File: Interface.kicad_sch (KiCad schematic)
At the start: 62 parts, among them U11 WE-TVS-82400102, U13 WE-TVS-82400102, U2 SN74LVC2G14DBV, U4 SN74LVC2G14DBV, U5 SN74LVC2G14DBV, U6 THVD1400D, U7 TLP2310, U8 TLP2310

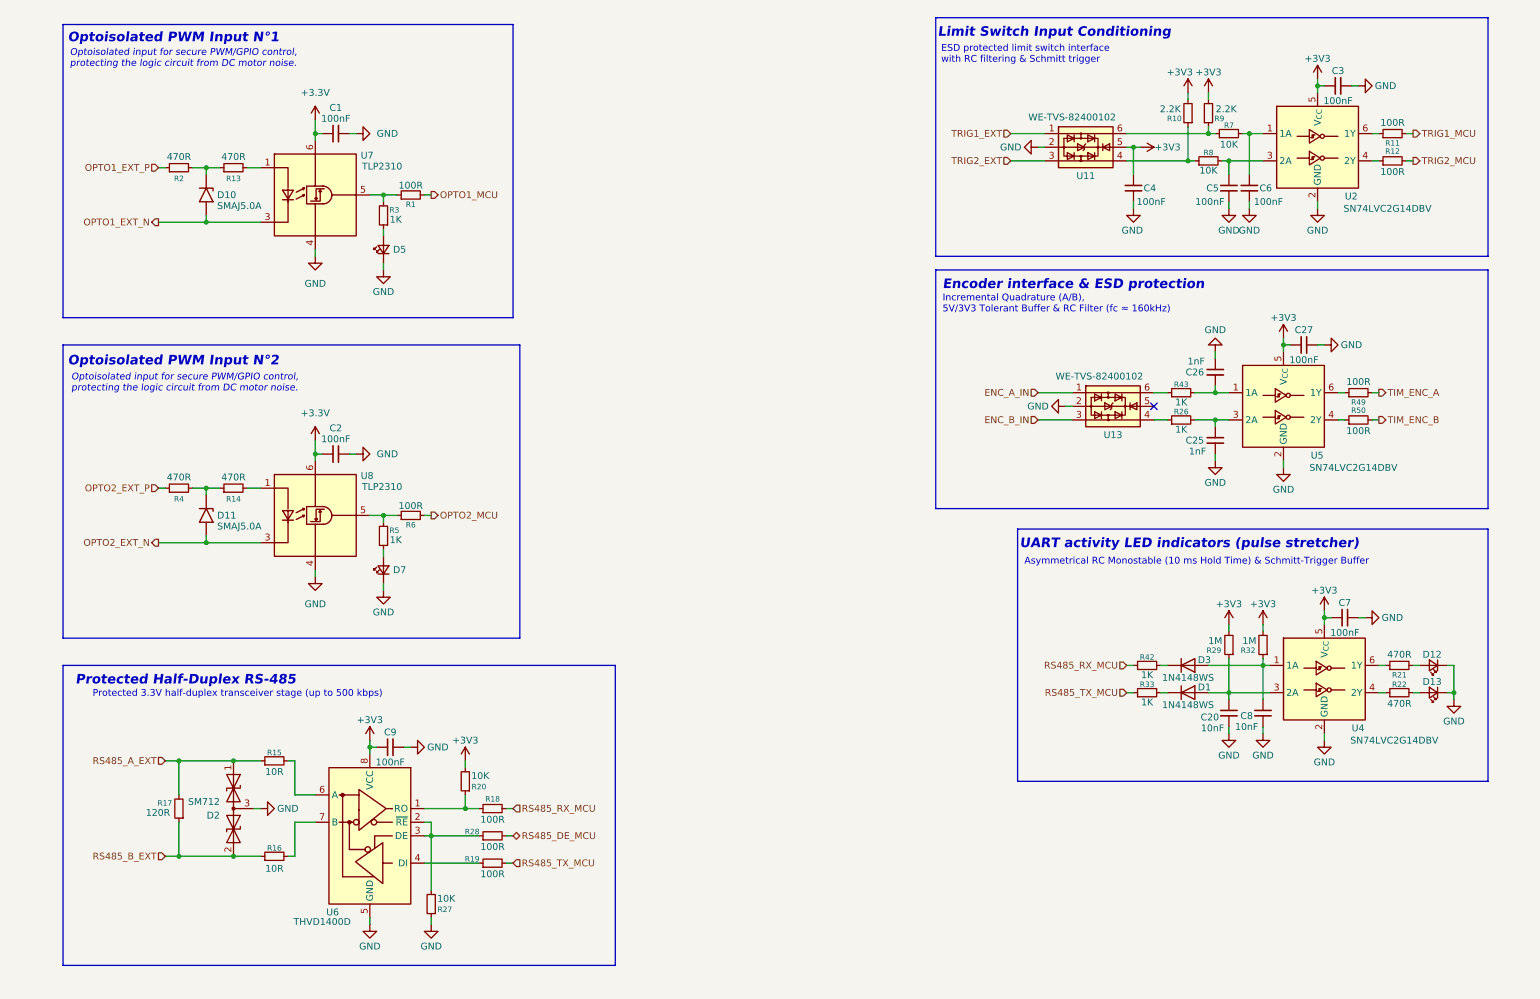
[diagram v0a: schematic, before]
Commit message: feat: add standardized functional notes across all schematic sheets
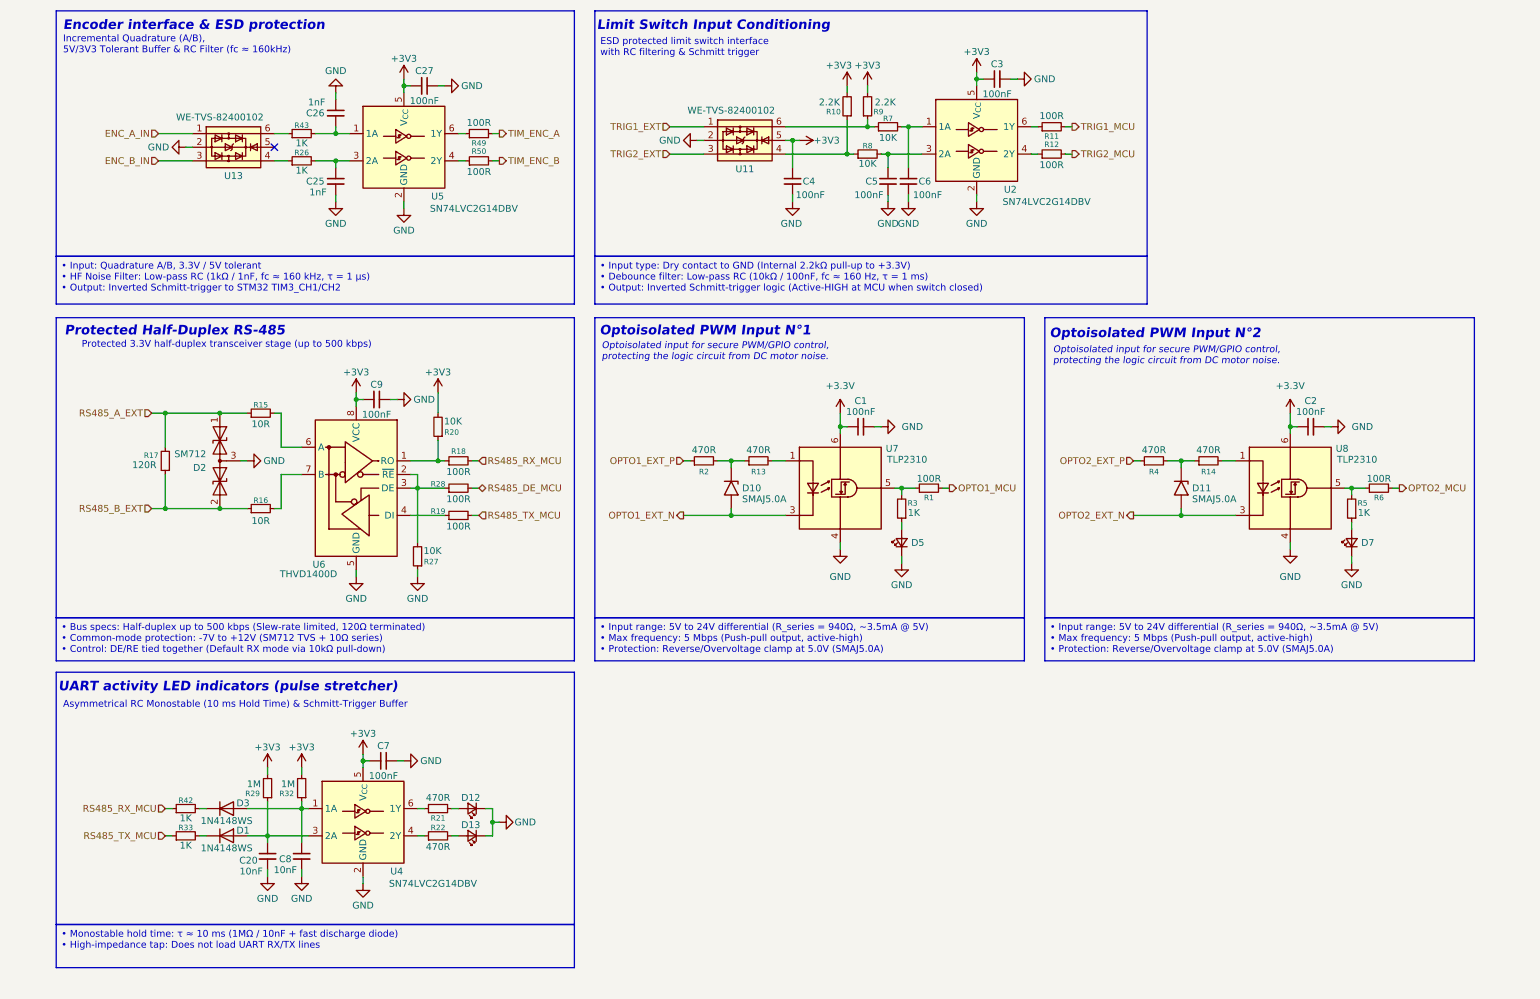
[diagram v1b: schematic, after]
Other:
- moved on the sheet: C1, C2, C20, C25, C26, C27, C3, C4, C5, C6, C7, C8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

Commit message: fix: fix some errors in shematic
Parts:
- D6: renamed from D10; value SMAJ5.0A -> SMAJ6.0A
- D8: renamed from D11; value SMAJ5.0A -> SMAJ6.0A
- R20: renamed from R2; value 470R -> 330R
- R21: renamed from R13; value 470R -> 330R
- R30: renamed from R4; value 470R -> 330R
- R31: renamed from R14; value 470R -> 330R
- renumbered C27 to C10, C4 to C11, C1 to C12, C5 to C13, C6 to C14, C3 to C15, C2 to C16, C20 to C4, C8 to C5, C26 to C6, C25 to C7, C9 to C8, C7 to C9, D2 to D1, D3 to D2, D1 to D3, D12 to D4, D13 to D5, D5 to D7, D7 to D9, R32 to R10, R27 to R11, R20 to R12, R21 to R13, R22 to R14, R18 to R15, R28 to R16, R19 to R17, R49 to R18, R50 to R19, R17 to R2, R10 to R22, R9 to R23, R8 to R24, R7 to R25, R3 to R26, R1 to R27, R11 to R28, R12 to R29, R42 to R3, R5 to R32, R6 to R33, R33 to R4, R15 to R5, R16 to R6, R29 to R7, R43 to R8, R26 to R9, U13 to U2, U6 to U3, U11 to U6, U2 to U8, U8 to U9
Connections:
- net +3.3V is gone; now on net +3V3: C12.1, C16.1, U7.6 (VDD), U9.6 (VDD)
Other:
- moved on the sheet: R27, R33

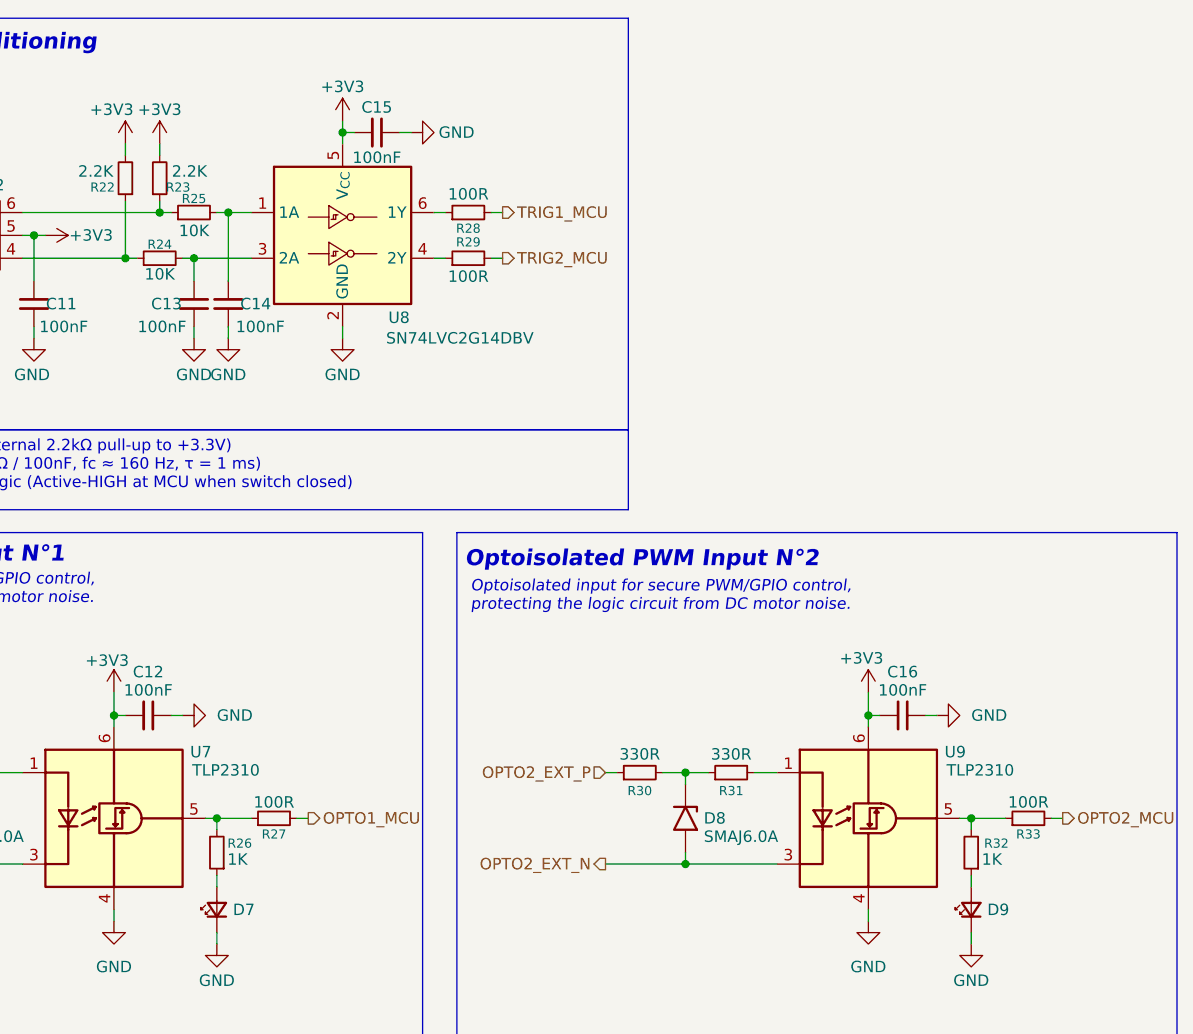
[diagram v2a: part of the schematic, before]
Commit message: fix : Fix the resitor value for leds
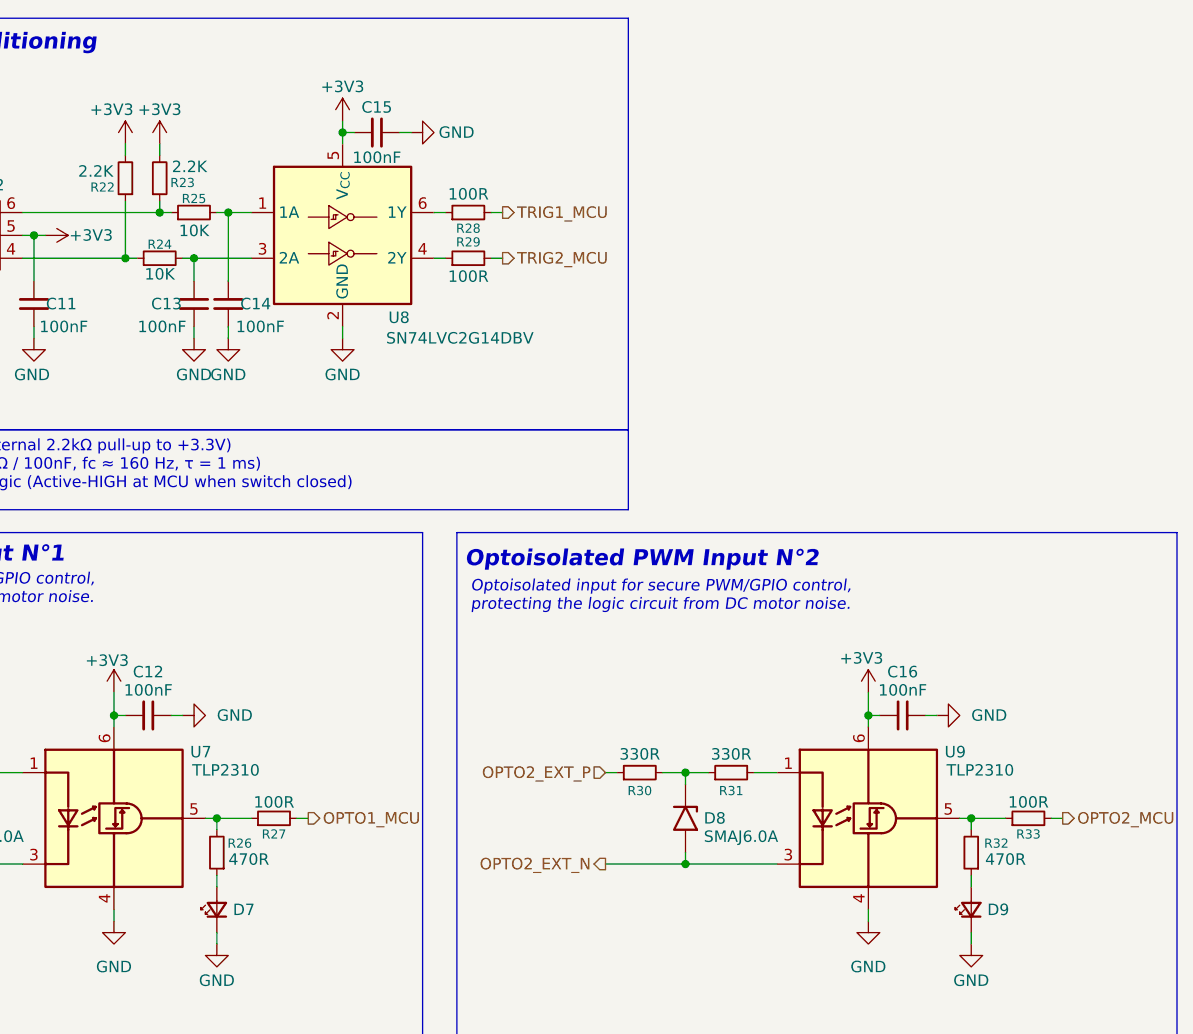
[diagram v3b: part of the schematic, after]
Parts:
- R26, R32: value 1K -> 470R
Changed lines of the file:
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@@
 			)
 		)
-		(property "Value" "1K"
-			(at 258.826 107.442 0)
+		(property "Value" "470R"
+			(at 260.35 107.442 0)
 			(show_name no)
 			(do_not_autoplace no)
@@
 		(dnp no)
 		(property "Reference" "R23"
-			(at 168.402 32.766 0)
+			(at 168.91 32.258 0)
 			(show_name no)
 			(do_not_autoplace no)
@@
 		)
 		(property "Value" "2.2K"
-			(at 169.672 30.988 0)
+			(at 169.672 30.48 0)
 			(show_name no)
 			(do_not_autoplace no)
@@
 			)
 		)
-		(property "Value" "1K"
-			(at 175.006 107.442 0)
+		(property "Value" "470R"
+			(at 176.276 107.442 0)
 			(show_name no)
 			(do_not_autoplace no)

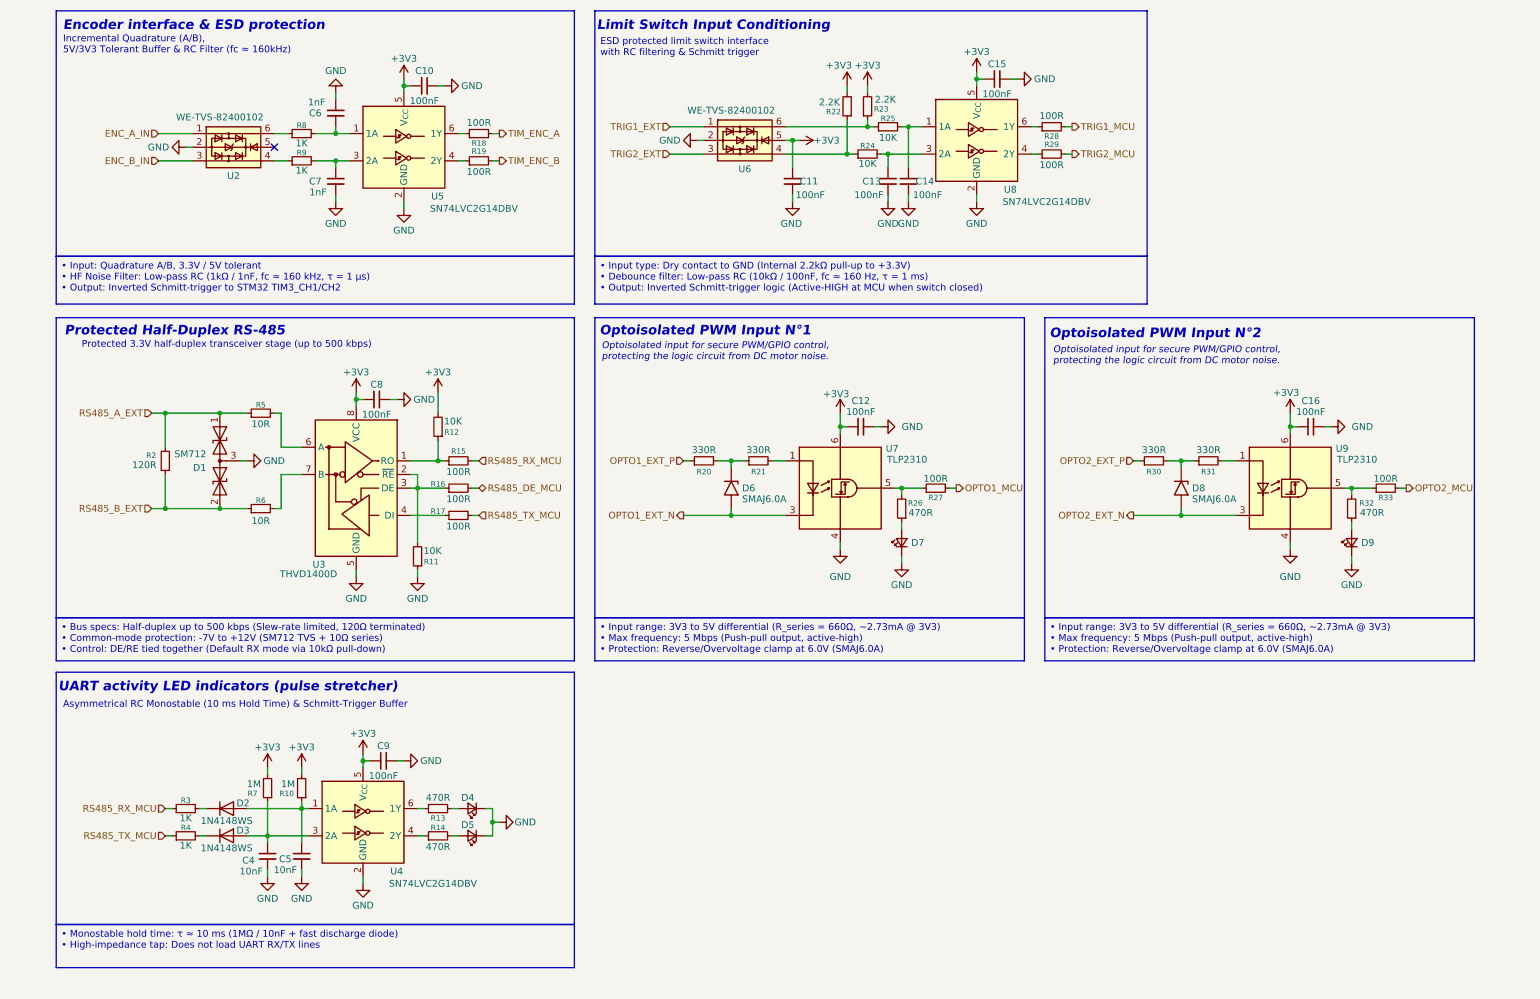
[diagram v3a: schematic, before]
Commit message: wip(sch): draft JST-XH and solder pad connector interfaces
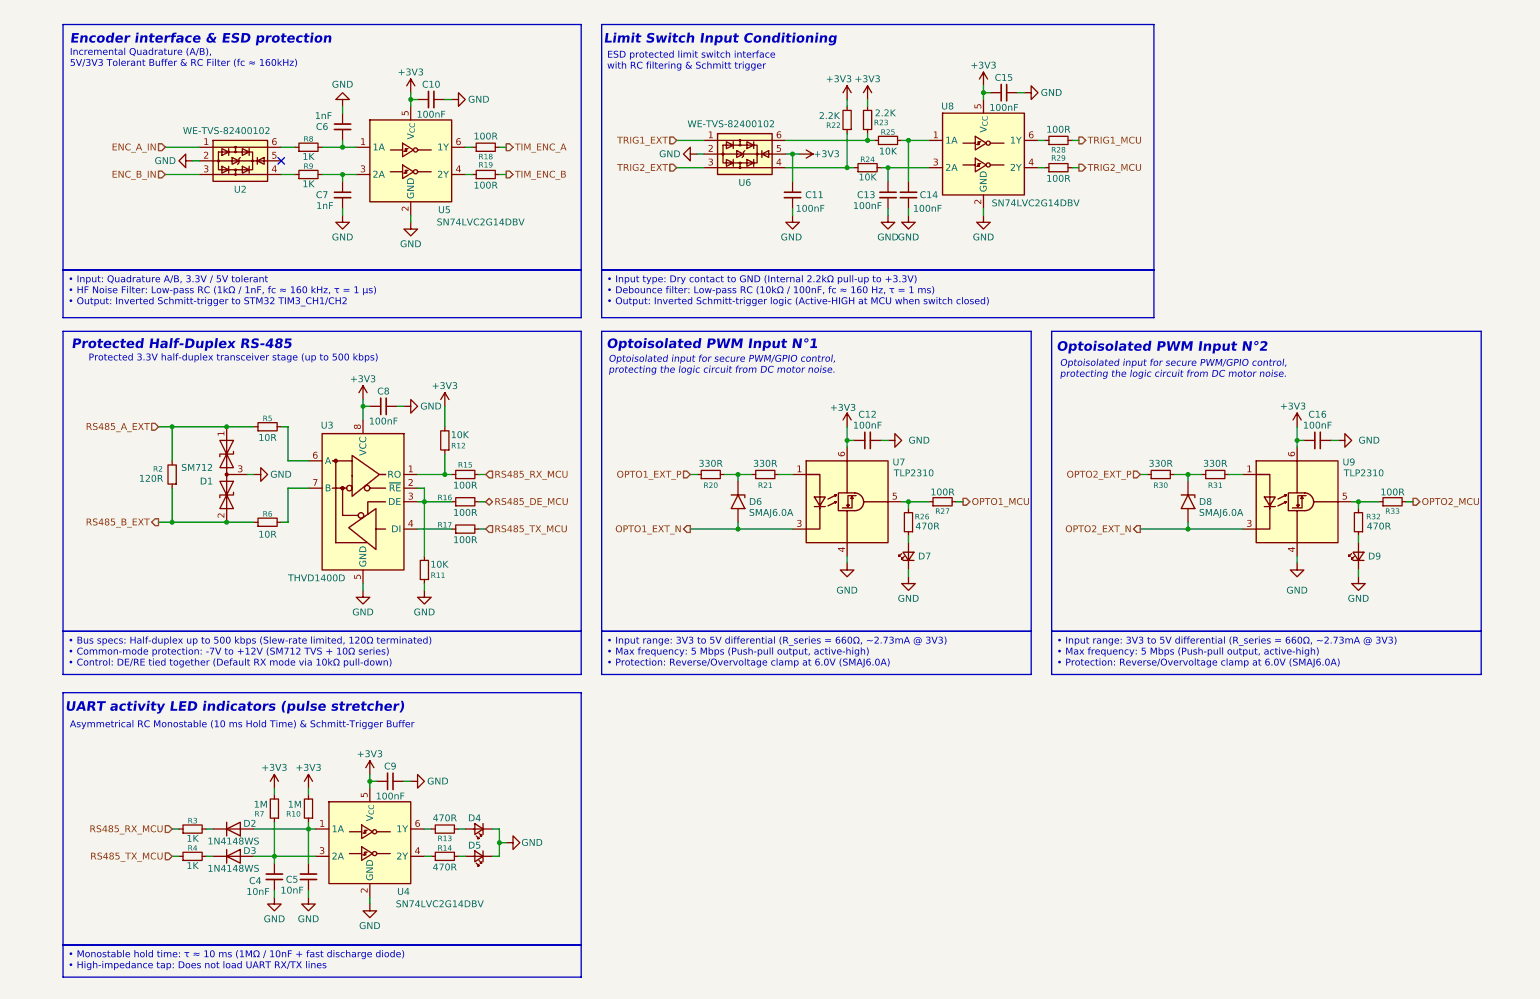
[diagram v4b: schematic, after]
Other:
- moved on the sheet: C10, C11, C12, C13, C14, C15, C16, C4, C5, C6, C7, C8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

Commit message: fix: FIx some modification
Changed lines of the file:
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@@
 	(wire
 		(pts
-			(xy 87.63 87.63) (xy 87.63 91.44)
+			(xy 87.63 86.36) (xy 87.63 91.44)
 		)
 		(stroke
@@
 	(symbol
 		(lib_id "power:+3V3")
-		(at 87.63 87.63 0)
+		(at 87.63 86.36 0)
 		(unit 1)
 		(body_style 1)
@@
 		(dnp no)
 		(property "Reference" "#PWR026"
-			(at 87.63 91.44 0)
+			(at 87.63 90.17 0)
 			(hide yes)
 			(show_name no)
@@
 		)
 		(property "Value" "+3V3"
-			(at 87.63 83.82 0)
+			(at 87.63 82.55 0)
 			(show_name no)
 			(do_not_autoplace no)
@@
 		)
 		(property "Footprint" ""
-			(at 87.63 87.63 0)
+			(at 87.63 86.36 0)
 			(hide yes)
 			(show_name no)
@@
 		)
 		(property "Datasheet" ""
-			(at 87.63 87.63 0)
+			(at 87.63 86.36 0)
 			(hide yes)
 			(show_name no)
@@
 		)
 		(property "Description" "Power symbol creates a global label with name \"+3V3\""
-			(at 87.63 87.63 0)
+			(at 87.63 86.36 0)
 			(hide yes)
 			(show_name no)
